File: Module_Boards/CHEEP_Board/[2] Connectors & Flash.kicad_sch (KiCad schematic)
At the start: 16 parts, among them U4 W25Q128JWYIQ

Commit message: Big push. Fixed the issues that were pending. See github
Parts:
- removed SW1: ~, X-MODs_PcbLib:TL1030AF160AQJ, symbol X-MODs_SchLib:TL1030AF160AQJ
- renumbered C15 to C14, C16 to C15, C17 to C16, C18 to C17, U4 to U2, U5 to U3, U6 to U4, U7 to U5
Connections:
- net +1V8: now also J1.18 (+1V8), J1.48 (+1V8); no longer J1.2 (+1V8), J1.20 (+1V8), J1.32 (+1V8), J1.52 (+1V8)
- net BOOT_SEL_EXT: now also J1.31 (BOOT_SEL_EXT); no longer J1.35 (BOOT_SEL_EXT)
- net FLASH_CS: now also J1.11 (FLASH_CS); no longer J1.14 (FLASH_CS)
- net FLASH_MISO: now also J1.10 (FLASH_MISO); no longer J1.13 (FLASH_MISO)
- net FLASH_MOSI: now also J1.9 (FLASH_MOSI); no longer J1.12 (FLASH_MOSI)
- net FLASH_SCK: now also J1.14 (FLASH_SCK); no longer J1.17 (FLASH_SCK)
- net FLASH_nHLD_nRST: now also J1.13 (FLASH_nHLD_nRST); no longer J1.16 (FLASH_nHLD_nRST)
- net FLASH_nWP: now also J1.12 (FLASH_nWP); no longer J1.15 (FLASH_nWP)
- net GND: now also J1.17 (GND), J1.20 (GND), J1.30 (GND), J1.49 (GND); no longer J1.22 (GND), J1.3 (GND), J1.34 (GND), J1.53 (GND)
- net GPIO_0: now also J1.58 (GPIO_0); no longer J1.62 (GPIO_0)
- net GPIO_1: now also J1.57 (GPIO_1); no longer J1.61 (GPIO_1)
- net GPIO_10: now also J1.45 (GPIO_10); no longer J1.49 (GPIO_10)
- net GPIO_11: now also J1.44 (GPIO_11); no longer J1.48 (GPIO_11)
- net GPIO_12: now also J1.43 (GPIO_12); no longer J1.47 (GPIO_12)
- net GPIO_13: now also J1.42 (GPIO_13); no longer J1.46 (GPIO_13)
- net GPIO_14: now also J1.41 (GPIO_14); no longer J1.45 (GPIO_14)
- net GPIO_15: now also J1.40 (GPIO_15); no longer J1.44 (GPIO_15)
- net GPIO_16: now also J1.39 (GPIO_16); no longer J1.43 (GPIO_16)
- net GPIO_17: now also J1.38 (GPIO_17); no longer J1.42 (GPIO_17)
- net GPIO_18: now also J1.37 (GPIO_18); no longer J1.41 (GPIO_18)
- net GPIO_19: now also J1.36 (GPIO_19); no longer J1.40 (GPIO_19)
- net GPIO_2: now also J1.56 (GPIO_2); no longer J1.60 (GPIO_2)
- net GPIO_20: now also J1.35 (GPIO_20); no longer J1.39 (GPIO_20)
- net GPIO_21: now also J1.34 (GPIO_21); no longer J1.38 (GPIO_21)
- net GPIO_22: now also J1.33 (GPIO_22); no longer J1.37 (GPIO_22)
- net GPIO_23: now also J1.32 (GPIO_23); no longer J1.36 (GPIO_23)
- net GPIO_3: now also J1.55 (GPIO_3); no longer J1.59 (GPIO_3)
- net GPIO_4: now also J1.54 (GPIO_4); no longer J1.58 (GPIO_4)
- net GPIO_5: now also J1.53 (GPIO_5); no longer J1.57 (GPIO_5)
- net GPIO_6: now also J1.52 (GPIO_6); no longer J1.56 (GPIO_6)
- net GPIO_7: now also J1.51 (GPIO_7); no longer J1.55 (GPIO_7)
- net GPIO_8: now also J1.50 (GPIO_8); no longer J1.54 (GPIO_8)
- net GPIO_9: now also J1.46 (GPIO_9); no longer J1.50 (GPIO_9)
- net I2C_SCL_HEEP: now also J1.16 (I2C_SCL_HEEP); no longer J1.19 (I2C_SCL_HEEP)
- net I2C_SDA_HEEP: now also J1.15 (I2C_SDA_HEEP); no longer J1.18 (I2C_SDA_HEEP)
- net JTAG_TCK: now also J1.5 (JTAG_TCK); no longer J1.8 (JTAG_TCK)
- net JTAG_TDI: now also J1.2 (JTAG_TDI); no longer J1.5 (JTAG_TDI)
- net JTAG_TDO: now also J1.1 (JTAG_TDO); no longer J1.4 (JTAG_TDO)
- net JTAG_TMS: now also J1.4 (JTAG_TMS); no longer J1.7 (JTAG_TMS)
- net JTAG_TRST: now also J1.3 (JTAG_TRST); no longer J1.6 (JTAG_TRST)
- net Manual_RST: now also J1.6 (Manual_RST); no longer J1.9 (Manual_RST)
- net PMIC_nRST: now also J1.7 (PMIC_nRST); no longer J1.10 (PMIC_nRST)
- net SOC_RST_OUT: now also J1.8 (SOC_RST_OUT); no longer J1.11 (SOC_RST_OUT)
- net SPI_CS0_HEEP: now also J1.28 (SPI_CS0_HEEP); no longer J1.30 (SPI_CS0_HEEP)
- net SPI_CS1_HEEP: now also J1.27 (SPI_CS1_HEEP); no longer J1.29 (SPI_CS1_HEEP)
- net SPI_MISO_HEEP: now also J1.24 (SPI_MISO_HEEP); no longer J1.26 (SPI_MISO_HEEP)
- net SPI_MOSI_HEEP: now also J1.23 (SPI_MOSI_HEEP); no longer J1.25 (SPI_MOSI_HEEP)
- net SPI_SCK_HEEP: now also J1.29 (SPI_SCK_HEEP); no longer J1.31 (SPI_SCK_HEEP)
- net SPI_SD2_HEEP: now also J1.25 (SPI_SD2_HEEP); no longer J1.27 (SPI_SD2_HEEP)
- net SPI_SD3_HEEP: now also J1.26 (SPI_SD3_HEEP); no longer J1.28 (SPI_SD3_HEEP)
- net UART_RX_HEEP: now also J1.21 (UART_RX_HEEP); no longer J1.23 (UART_RX_HEEP)
- net UART_TX_HEEP: now also J1.22 (UART_TX_HEEP); no longer J1.24 (UART_TX_HEEP)
- net VCORE: now also J1.19 (VCORE), J1.47 (VCORE); no longer J1.1 (VCORE), J1.21 (VCORE), J1.33 (VCORE), J1.51 (VCORE)
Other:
- moved on the sheet: R8, R9, U3A, U3B, U4A, U5A

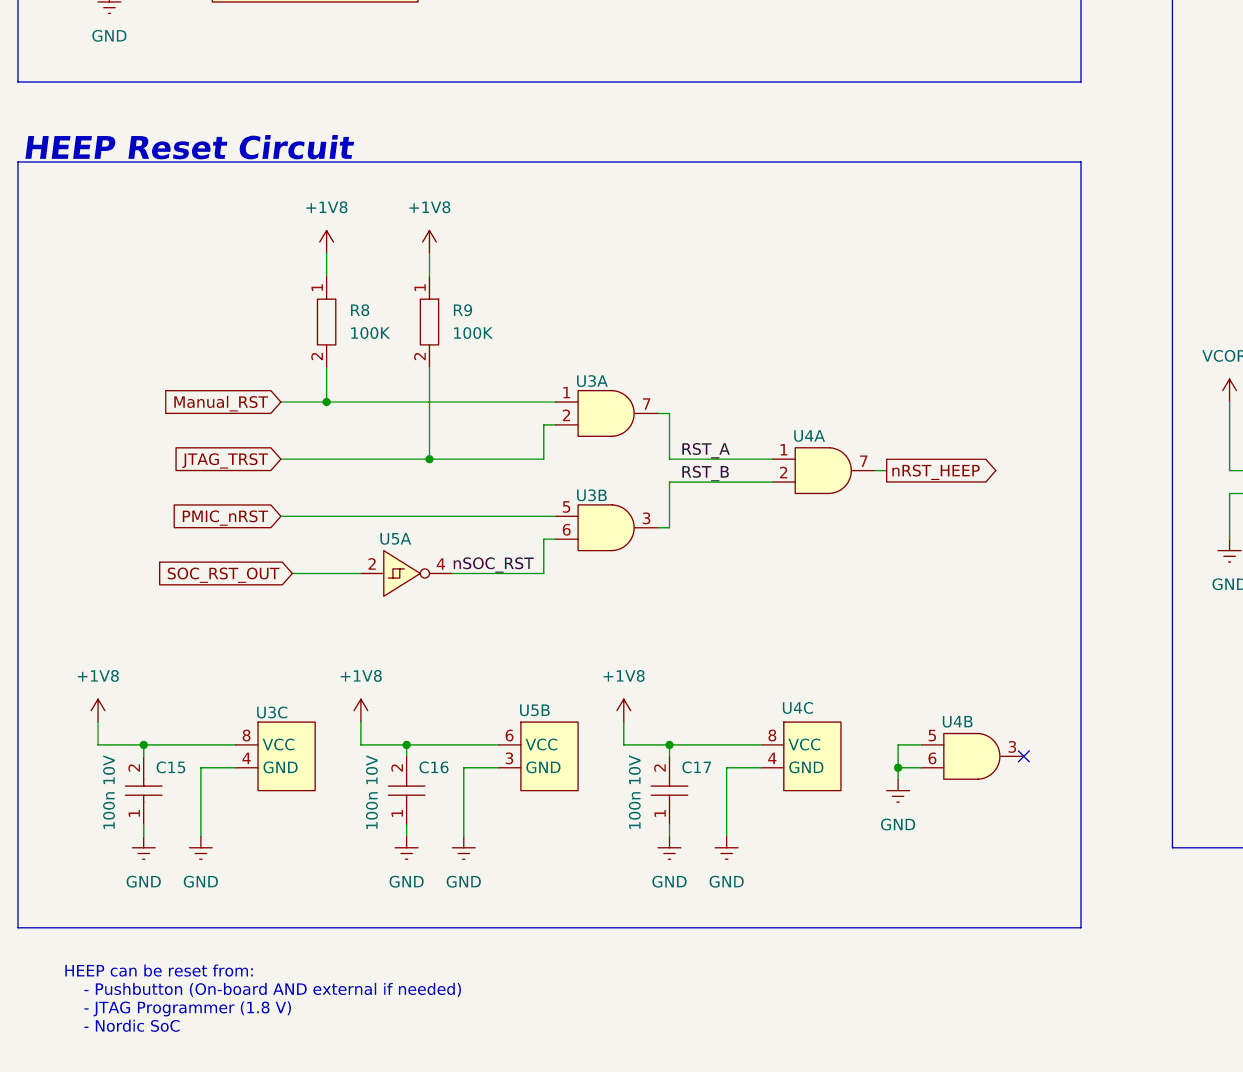
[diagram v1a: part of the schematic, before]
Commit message: Fixed bugs. Added comments. Push before changing the ADC
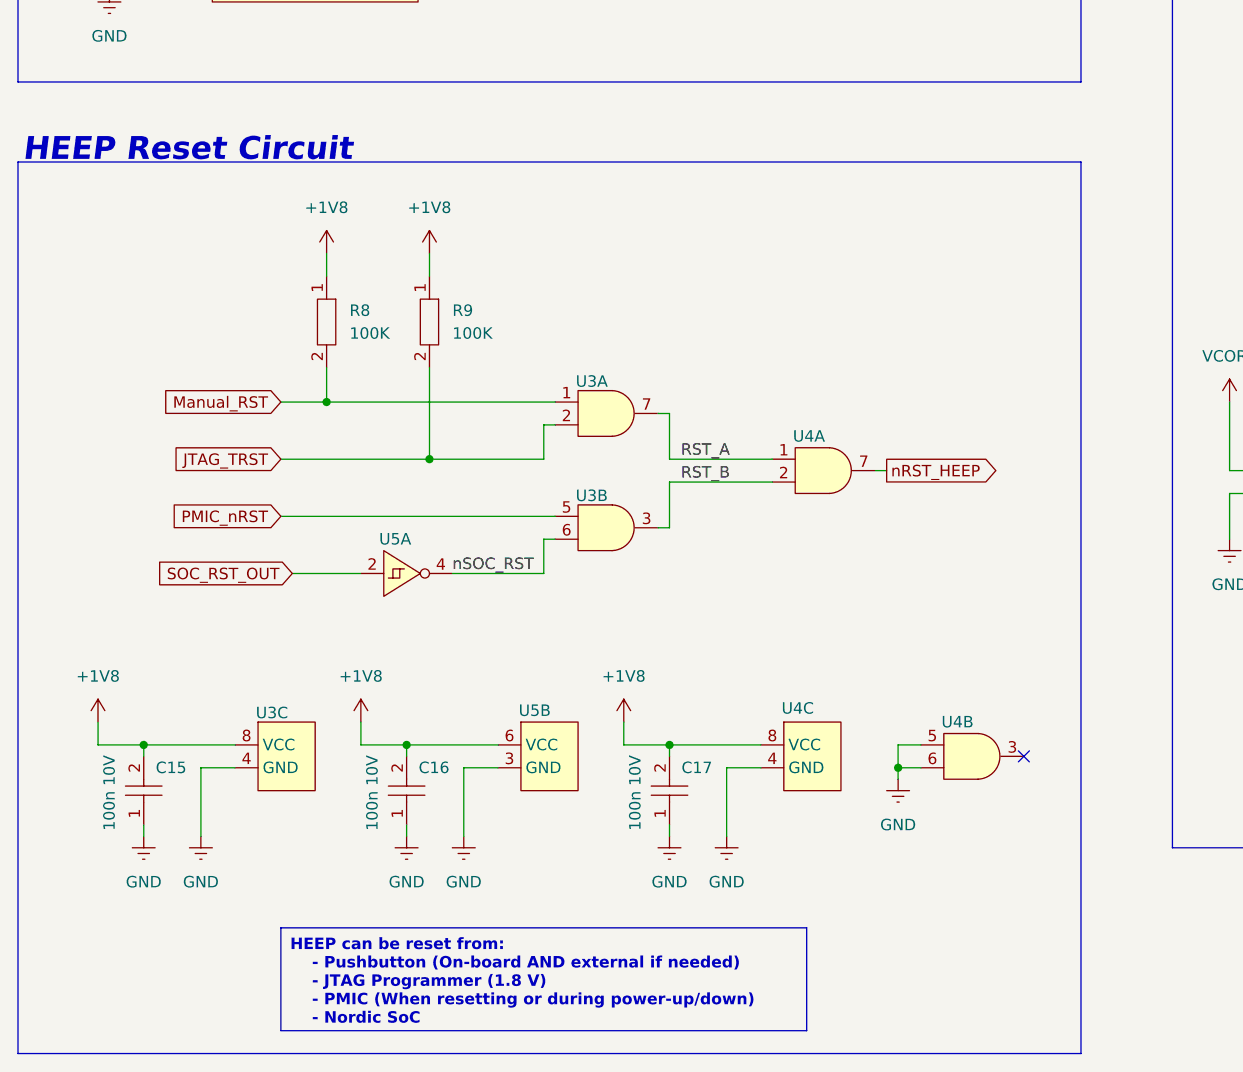
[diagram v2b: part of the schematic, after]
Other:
- note removed: "HEEP can be reset from: - Pushbutton (On-board AND external if needed) - JTAG Programmer (1.8 V) - Nordic SoC"
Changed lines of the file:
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@@
 	(rectangle
 		(start 24.13 87.63)
-		(end 142.24 172.72)
+		(end 142.24 186.69)
 		(stroke
 			(width 0)
@@
 		(fill
 			(type none)
+		)
+	)
+	(text_box "HEEP can be reset from:\n	- Pushbutton (On-board AND external if needed)\n	- JTAG Programmer (1.8 V)\n	- PMIC (When resetting or during power-up/down)\n	- Nordic SoC"
+		(exclude_from_sim no)
+		(at 53.34 172.72 0)
+		(size 58.42 11.43)
+		(stroke
+			(width 0)
+			(type default)
+		)
+		(fill
+			(type color)
+			(color 255 255 150 1)
+		)
+		(effects
+			(font
+				(size 1.27 1.27)
+				(thickness 0.254)
+				(bold yes)
+				(color 255 2 0 1)
+			)
+			(justify left top)
 		)
 	)
@@
 			)
 			(justify left)
-		)
-	)
-	(text "HEEP can be reset from:\n	- Pushbutton (On-board AND external if needed)\n	- JTAG Programmer (1.8 V)\n	- Nordic SoC"
-		(exclude_from_sim no)
-		(at 29.21 180.848 0)
-		(effects
-			(font
-				(face "KiCad Font")
-				(size 1.27 1.27)
-			)
-			(justify left)

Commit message: Final revision and production files
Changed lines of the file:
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@@
 	)
 	(global_label "JTAG_TCK"
-		(shape input)
+		(shape bidirectional)
 		(at 186.69 53.34 180)
 		(fields_autoplaced yes)

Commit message: Push with updated readme
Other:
- company: (none) -> Embedded Systems Laboratory - EPFL
- title: (none) -> [2] Connectors & Flash
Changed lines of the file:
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@@
 	(generator_version "8.0")
 	(paper "A4")
+	(title_block
+		(title "[2] Connectors & Flash")
+		(rev "1.0")
+		(company "Embedded Systems Laboratory - EPFL")
+		(comment 1 "Author: José Angel Miranda Calero")
+		(comment 2 "Author: Juan Sapriza")
+		(comment 3 "Author: Alejandro López Rodriguez")
+	)
 	(junction
 		(at 87.63 53.34)
